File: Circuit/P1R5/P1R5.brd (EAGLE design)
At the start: 50.8 x 50.8 mm, 182 parts, among them J1 2X5_0.05"_CORTEX_DEBUGTH_NOKE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, U1 MK20DX256VLH7, U2 TPS61200, U3 PCA9552BS, U4 PCA9552BS, U5 MPU-9250, U6 ESP8266EX, U7 25Q40, U8 NRF24L01, Y1 8MHz, Y2 34.728kHz, Y3 26 Mhz, Y4 16 Mhz

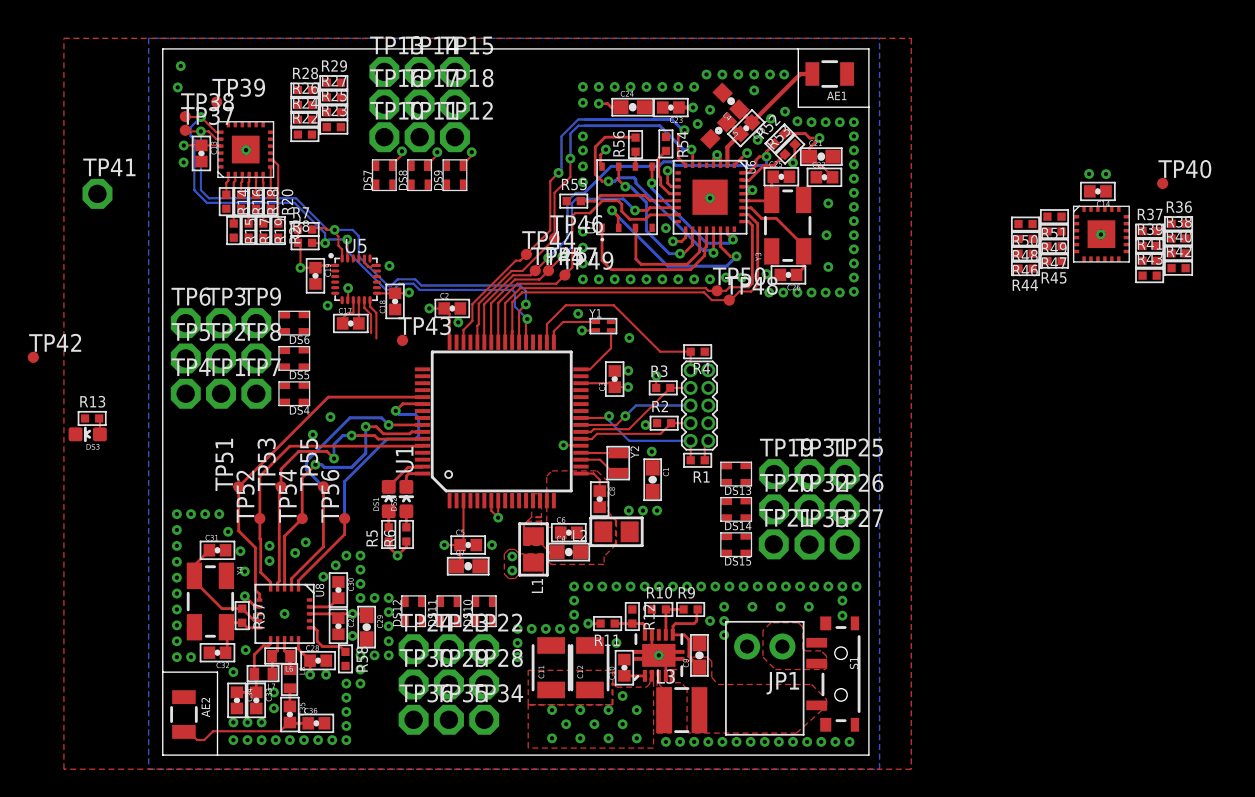
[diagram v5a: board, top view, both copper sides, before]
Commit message: More board layout. Renumbered x+ and y+ to match what I did on the PCB.
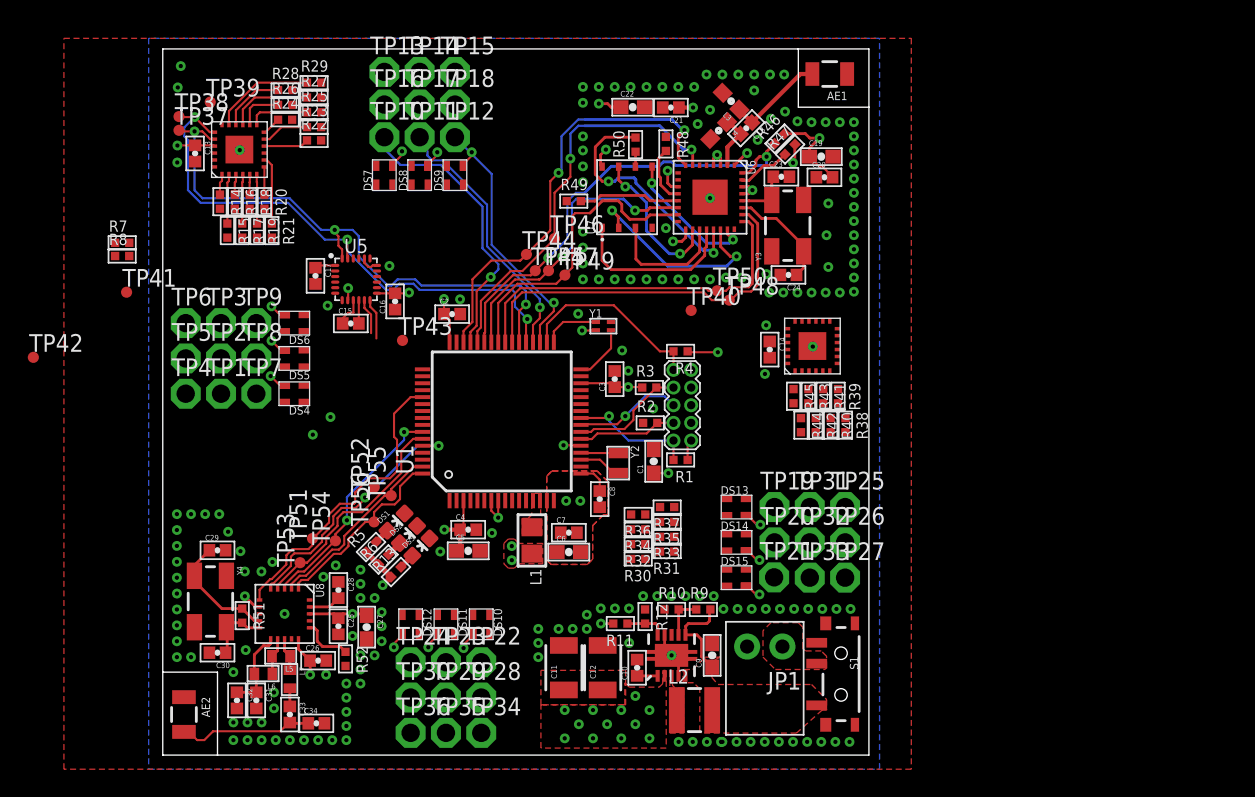
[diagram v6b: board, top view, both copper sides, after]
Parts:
- removed C35: 1.5 pF, SparkFun-Capacitors:0402-CAP
- removed C36: 1.0 pF, SparkFun-Capacitors:0402-CAP
- removed L8: 3.9 nH, SparkFun-Passives:C0402
- removed R53, R54: 12k, appfruits:_0402
- removed R55: 10k, appfruits:_0402
- removed R56: 200, appfruits:_0402
- removed R57: 1M, appfruits:_0402
- removed R58: 22k, appfruits:_0402
- added C15, C16: 0.1 uF, SparkFun-Capacitors:0402-CAP
- added R30, R31, R32, R33, R34, R35: 86.6, appfruits:_0402
- C18: value 0.1 uF -> 5.6 pF
- C19, C22, C27: value 0.1 uF -> 10uF; device SparkFun-Capacitors:0402-CAP -> SparkFun-Capacitors:0603-CAP
- C20: value 5.6 pF -> 0.1 uF
- C21: value 10uF -> 0.1 uF; device SparkFun-Capacitors:0603-CAP -> SparkFun-Capacitors:0402-CAP
- C23: value 0.1 uF -> 15 pF
- C24: value 10uF -> 15 pF; device SparkFun-Capacitors:0603-CAP -> SparkFun-Capacitors:0402-CAP
- C25, C26: value 15 pF -> 0.1 uF
- C28: value 0.1 uF -> .033 uF
- C29: value 10uF -> 22 pF; device SparkFun-Capacitors:0603-CAP -> SparkFun-Capacitors:0402-CAP
- C30: value .033 uF -> 22 pF
- C31: value 22 pF -> 2200 pF
- C32: value 22 pF -> 4.7 pF
- C33: value 2200 pF -> 1.5 pF
- C34: value 4.7 pF -> 1.0 pF
- C4, C7: value 10uF -> 0.1uF; device SparkFun-Capacitors:0603-CAP -> SparkFun-Capacitors:0402-CAP
- C5, C6: value 0.1uF -> 10uF; device SparkFun-Capacitors:0402-CAP -> SparkFun-Capacitors:0603-CAP
- L2: value 600 Ohm/100 Mhz -> 2.2uH, 1.4A; device appfruits:0805 -> appfruits:LPS3015
- L3: value 2.2uH, 1.4A -> DNP; device appfruits:LPS3015 -> SparkFun-Passives:0603
- L5: value DNP -> 8.2 nH; device SparkFun-Passives:0603 -> SparkFun-Passives:C0402
- L6: value 8.2 nH -> 2.7 nH
- L7: value 2.7 nH -> 3.9 nH
- R46, R47, R48: value 86.6 -> 12k
- R49: value 86.6 -> 10k
- R50: value 86.6 -> 200
- R51: value 86.6 -> 1M
- R52: value 12k -> 22k
- TP41: value TPPAD1-13 -> TPTP08R; device testpad:P1-13 -> testpad:TP08R
- moved R51 65.1 mm to (5.71, 10.0), turned to 270 degrees
- moved L5 49.2 mm to (8.51, 7.11), turned to 180 degrees
- moved R52 48.7 mm to (13.1, 6.92), turned to 270 degrees
- moved C25 45.4 mm to (12.6, 9.27), turned to 270 degrees
- moved R36 44.1 mm to (34.2, 17.3), turned to 180 degrees
- moved L3 43.9 mm to (40.9, 47.0), turned to 135 degrees
- moved C26 43.8 mm to (11.2, 6.79), turned to 0 degrees
- moved R37 40.0 mm to (36.3, 17.8), turned to 180 degrees
- moved C19 37.4 mm to (47.4, 43.1), turned to 0 degrees
- moved TP40 35.1 mm to (38.0, 32.0)
- moved R49 34.7 mm to (29.6, 39.9), turned to 0 degrees
- moved R50 28.6 mm to (34.0, 43.9), turned to 90 degrees
- moved R42 28.4 mm to (47.0, 23.7), turned to 270 degrees
- moved C18 28.2 mm to (42.0, 45.1), turned to 225 degrees
- moved R40 27.9 mm to (48.0, 23.7), turned to 270 degrees
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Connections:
- removed net AGND: C4.2, C6.2, C8.2, L2.2, U1.15, U1.16
- net !CS: now also U1.49; no longer U1.45
- net !RESET0: now also U1.55; no longer U1.26
- net 3.3V: now also C16.2, C17.1, C20.2, C22.1, C25.1, C26.1, C4.1, R46.2; no longer C18.2, C22.2, C23.1, C24.1, C28.1, C29.1, C7.1, R52.2
- net CE: now also U1.64; no longer U1.54
- net CLK: now also R50.1; no longer R56.1
- net CSN: now also U1.63; no longer U1.57
- net FSYNC: now also U1.56; no longer U1.36
- net GND: now also C15.1, C16.1, C17.2, C20.1, C22.2, C28.1, C30.2, C4.2, C6.2, C8.2, L3.2, R47.2, R48.1, R49.1, R52.2, U1.15, U1.16; no longer C17.1, C18.1, C22.1, C28.2, C30.1, C33.2, C36.2, L2.1, L5.2, R53.2, R54.1, R55.1, R58.2
- net INT: now also U1.54; no longer U1.35
- net N$10: now also U1.57; no longer U1.63
- net N$100: now also C23.1; no longer C25.1
- net N$101: now also C18.1, L3.1; no longer C20.1, L4.1
- net N$102: now also R48.2; no longer R54.2
- net N$103: now also R49.2; no longer R55.2
- net N$107: now also R47.1; no longer R53.1
- net N$108: now also C29.1, R51.1; no longer C31.1, R57.1
- net N$109: now also C30.1, R51.2; no longer C32.1, R57.2
- net N$111: now also L5.1, L7.1; no longer L6.1, L8.1
- net N$112: now also R52.1; no longer R58.1
- net N$113: now also C28.2; no longer C30.2
- net N$114: now also L5.2, L6.1; no longer L6.2, L7.1
- net N$115: now also C33.2, C34.1; no longer C35.2, C36.1
- net N$116: now also C33.1, L7.2; no longer C35.1, L8.2
- net N$117: now also C31.1, C32.1, L6.2; no longer C33.1, C34.1, L7.2
- net N$12: now also U1.45; no longer U1.62
- net N$13: now also U1.61; no longer U1.64
- net N$14: now also U1.36; no longer U1.61
- net N$15: now also U1.35; no longer U1.49
- net N$16: now also U1.62; no longer U1.56
- net N$17: now also U1.26; no longer U1.55
- net N$18: now also U1.2; no longer U1.1
- net N$19: now also U1.1; no longer U1.2
- net N$22: now also C18.2, L4.1; no longer C20.2, L5.1
- net N$23: now also C24.1; no longer C26.1
- net N$24: now also L2.1; no longer L3.1
- net N$3: now also R50.2; no longer R56.2
- net N$4: now also C15.2; no longer C17.2
- net N$42: now also R31.2; no longer R37.2
- net N$43: now also R30.2; no longer R36.2
- net N$50: now also R40.2; no longer R46.2
- net N$52: now also R33.2; no longer R39.2
- net N$57: now also R45.2; no longer R51.2
- net N$58: now also R35.2; no longer R41.2
- net N$59: now also R39.2; no longer R45.2
- net N$61: now also R34.2; no longer R40.2
- net N$62: now also R42.2; no longer R48.2
- net N$63: now also R32.2; no longer R38.2
- net N$64: now also R37.2; no longer R43.2
- net N$67: now also R41.2; no longer R47.2
- net N$68: now also R38.2; no longer R44.2
- net N$70: now also R43.2; no longer R49.2
- net N$82: now also R36.2; no longer R42.2
- net N$83: now also R44.2; no longer R50.2
- net N$84: now also R30.1; no longer R36.1
- net N$85: now also R31.1; no longer R37.1
- net N$86: now also R32.1; no longer R38.1
- net N$87: now also R33.1; no longer R39.1
- net N$88: now also R34.1; no longer R40.1
- net N$89: now also R35.1; no longer R41.1
- net N$90: now also R36.1; no longer R42.1
- net N$91: now also R37.1; no longer R43.1
- net N$92: now also R38.1; no longer R44.1
- net N$93: now also R39.1; no longer R45.1
- net N$94: now also R40.1; no longer R46.1
- net N$95: now also R41.1; no longer R47.1
- net N$96: now also R42.1; no longer R48.1
- net N$97: now also R43.1; no longer R49.1
- net N$98: now also R44.1; no longer R50.1
- net N$99: now also R45.1; no longer R51.1
- net VDDA: now also C7.1; no longer C4.1
- net V_IN: now also L2.2; no longer L3.2
- net WIFI_RESET: now also R46.1; no longer R52.1
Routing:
- net N$12: track 0.00 -> 20.7 mm, vias 0 -> 1
- net N$14: track 0.00 -> 19.0 mm, vias 0 -> 1
- net N$15: track 0.00 -> 18.3 mm, vias 0 -> 1
- net 3.3V: track 66.6 -> 76.9 mm, vias 43 -> 51
- net N$81: track 0.00 -> 7.43 mm
- net CE: track 21.1 -> 13.9 mm, vias 1 -> 0
- net CSN: track 20.5 -> 13.9 mm, vias 1 -> 0
- net N$79: track 0.00 -> 6.06 mm
- net N$80: track 0.00 -> 4.66 mm
- net MOSI: track 21.0 -> 16.6 mm, vias 2 -> 0
- net N$77: track 0.00 -> 4.36 mm
- net SCK: track 20.2 -> 16.5 mm
- net N$75: track 0.00 -> 3.42 mm
- net N$78: track 0.00 -> 3.30 mm
- net N$74: track 0.00 -> 3.23 mm
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- added copper zone on layer 1, net N$1000
- removed copper zone on layer 1, net AGND

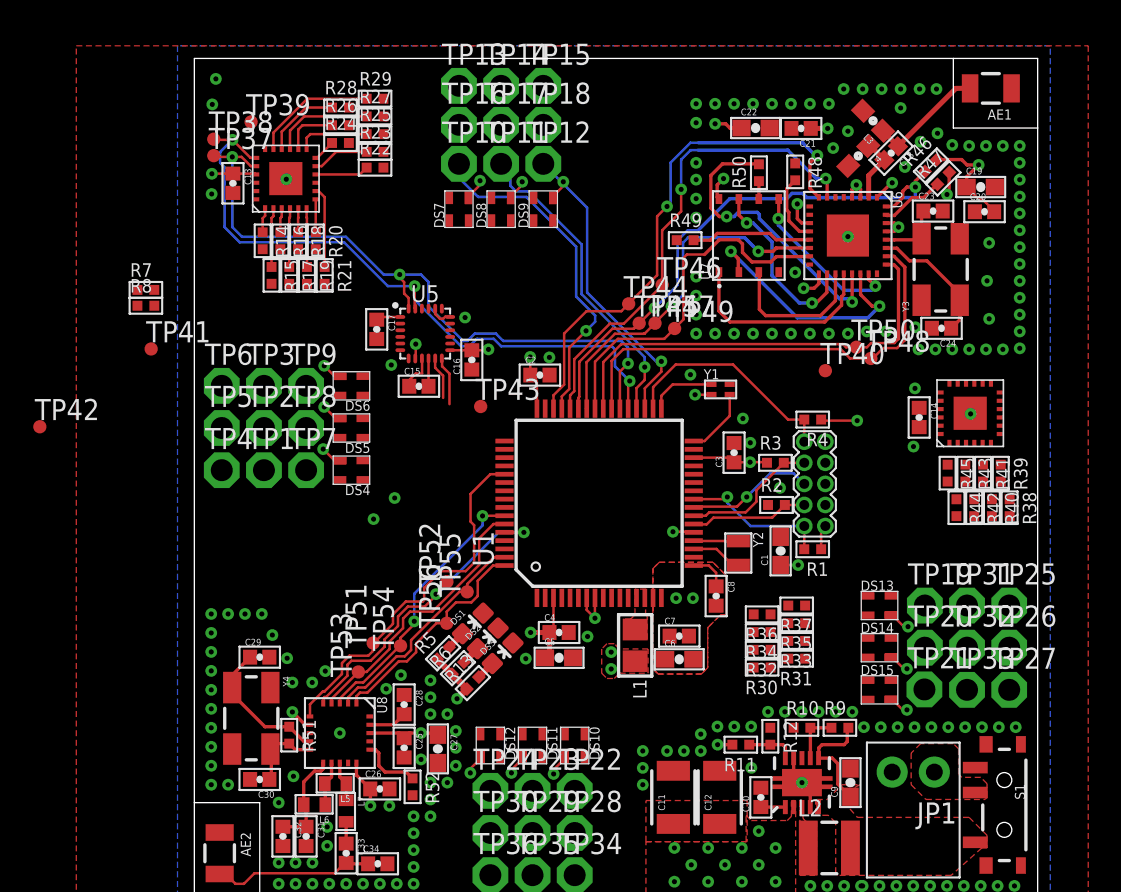
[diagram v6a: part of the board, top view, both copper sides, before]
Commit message: Everything but 3 banks of LED's is routed.
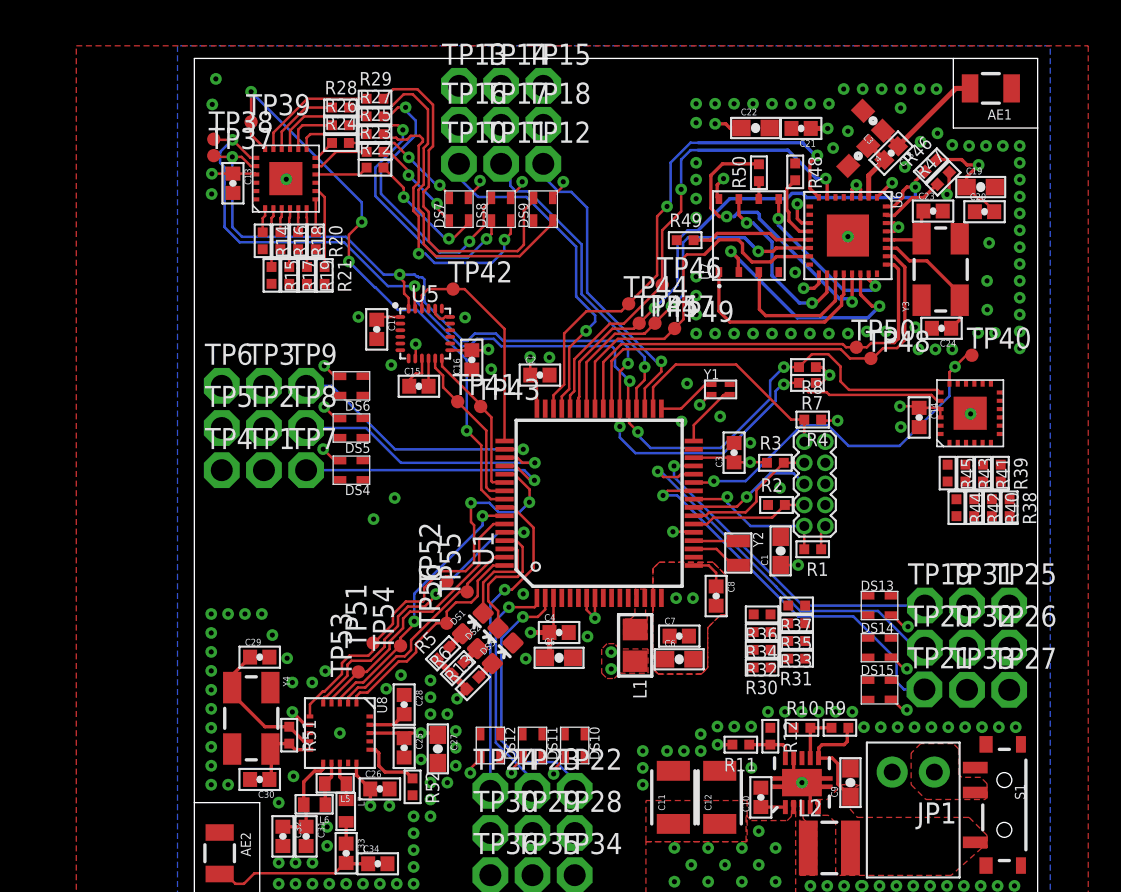
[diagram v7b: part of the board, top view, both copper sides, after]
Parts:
- moved R7 40.2 mm to (36.9, 31.3), turned to 180 degrees
- moved R8 40.0 mm to (36.9, 32.2), turned to 180 degrees
- moved TP42 26.2 mm to (15.6, 36.9)
- moved TP41 18.7 mm to (15.9, 30.1)
- moved TP40 8.88 mm to (46.8, 32.9)
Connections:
- net !RESET0: now also U1.56; no longer U1.55
- net 3.3V: now also DS10.4, DS11.4, DS12.4, DS13.4, DS14.4, DS15.4, DS4.4, DS5.4, DS6.4, DS7.4, DS8.4, DS9.4; no longer DS10.V, DS11.V, DS12.V, DS13.V, DS14.V, DS15.V, DS4.V, DS5.V, DS6.V, DS7.V, DS8.V, DS9.V
- net FSYNC: now also U1.55; no longer U1.56
- net N$10: now also U1.62; no longer U1.57
- net N$16: now also U1.57; no longer U1.62
- net N$20: now also TP19.TP; no longer TP20.TP
- net N$21: now also TP20.TP; no longer TP19.TP
- net N$36: now also DS8.2; no longer DS8.R
- net N$37: now also DS7.2; no longer DS7.R
- net N$38: now also DS7.1; no longer DS7.B
- net N$39: now also DS7.3; no longer DS7.G
- net N$40: now also DS8.1; no longer DS8.B
- net N$41: now also DS8.3; no longer DS8.G
- net N$42: now also DS10.3; no longer DS10.G
- net N$43: now also DS10.1; no longer DS10.B
- net N$44: now also DS9.1; no longer DS9.B
- net N$45: now also DS9.3; no longer DS9.G
- net N$47: now also DS5.2; no longer DS5.R
- net N$50: now also DS14.1; no longer DS14.B
- net N$51: now also DS4.2; no longer DS4.R
- net N$52: now also DS11.2; no longer DS11.R
- net N$53: now also DS4.1; no longer DS4.B
- net N$54: now also DS4.3; no longer DS4.G
- net N$55: now also DS5.1; no longer DS5.B
- net N$56: now also DS5.3; no longer DS5.G
- net N$57: now also DS15.3; no longer DS15.G
- net N$58: now also DS12.1; no longer DS12.B
- net N$59: now also DS13.3; no longer DS13.G
- net N$61: now also DS11.3; no longer DS11.G
- net N$62: now also DS14.3; no longer DS14.G
- net N$63: now also DS11.1; no longer DS11.B
- net N$64: now also DS12.3; no longer DS12.G
- net N$65: now also DS6.1; no longer DS6.B
- net N$66: now also DS6.3; no longer DS6.G
- net N$67: now also DS14.2; no longer DS14.R
- net N$68: now also DS13.1; no longer DS13.B
- net N$70: now also DS15.1; no longer DS15.B
- net N$82: now also DS12.2; no longer DS12.R
- net N$83: now also DS15.2; no longer DS15.R
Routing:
- net !RESET0: track 0.00 -> 36.5 mm, vias 0 -> 4
- net SCL: track 41.5 -> 66.3 mm, vias 3 -> 5
- net SDA: track 41.3 -> 65.2 mm, vias 3 -> 5
- net N$17: track 0.00 -> 23.3 mm, vias 0 -> 1
- net N$45: track 0.00 -> 23.0 mm
- net !RESET1: track 0.00 -> 23.0 mm, vias 0 -> 2
- net N$21: track 0.00 -> 22.9 mm, vias 0 -> 1
- net N$44: track 0.00 -> 21.4 mm
- net N$20: track 0.00 -> 20.2 mm, vias 0 -> 1
- net N$16: track 0.00 -> 19.4 mm, vias 0 -> 1
- net N$40: track 0.00 -> 18.2 mm, vias 0 -> 2
- net N$36: track 0.00 -> 18.0 mm, vias 0 -> 2
- net N$41: track 0.00 -> 17.6 mm, vias 0 -> 2
- net N$6: track 0.00 -> 16.6 mm, vias 0 -> 1
- net N$18: track 0.00 -> 16.3 mm, vias 0 -> 1
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
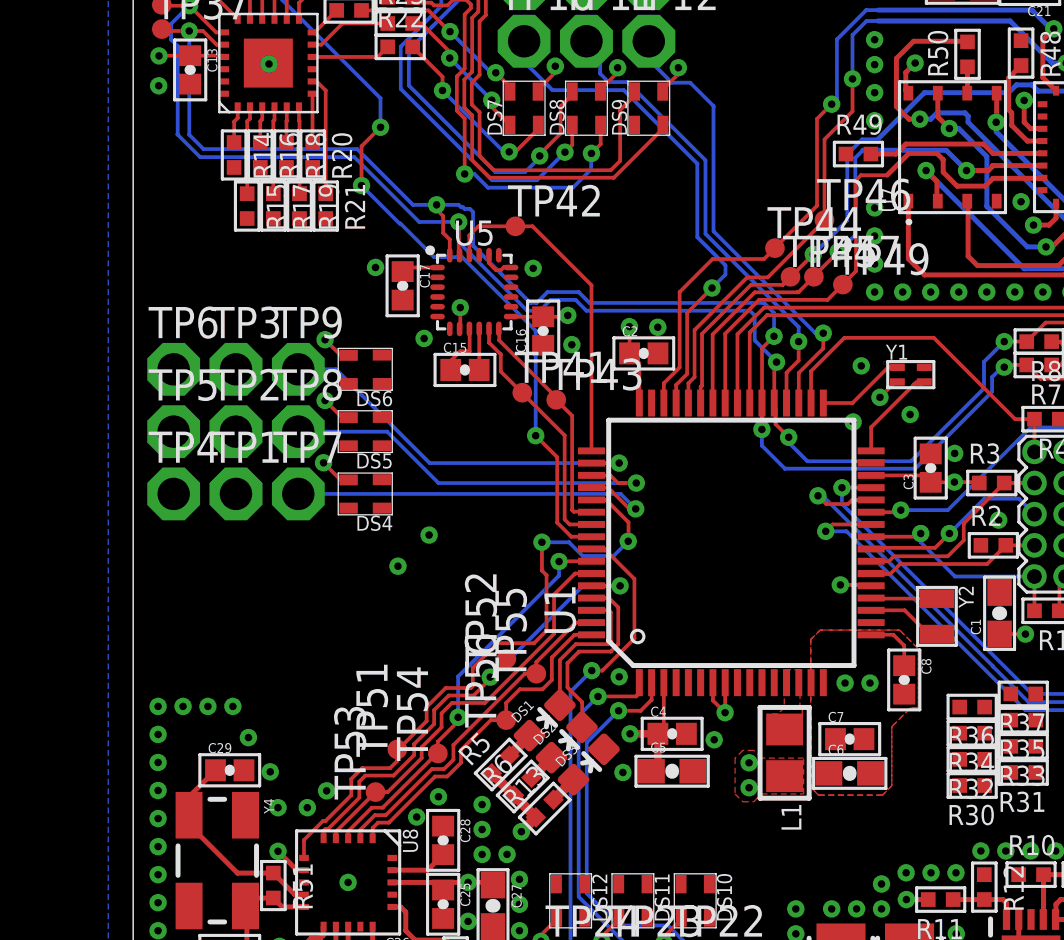
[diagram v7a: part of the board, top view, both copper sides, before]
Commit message: Routed another bank of LED's moved IMU up and to the right a bit.
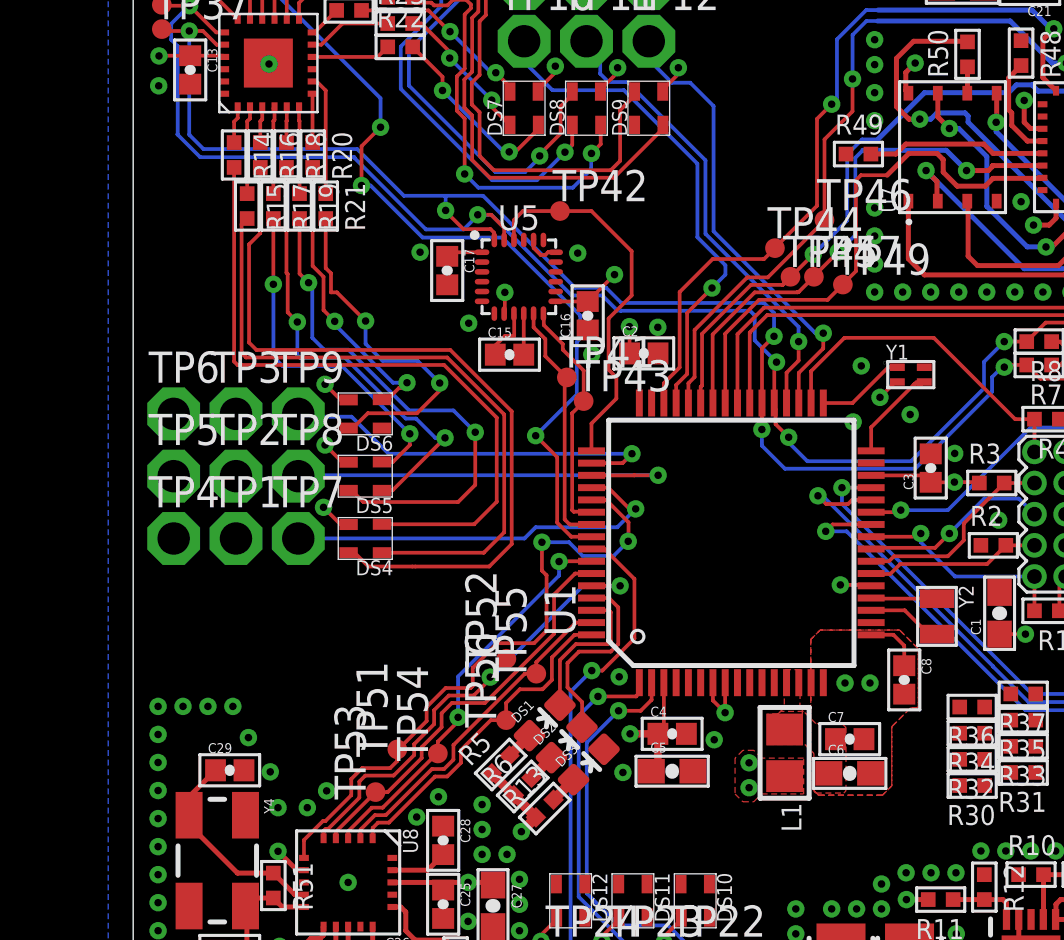
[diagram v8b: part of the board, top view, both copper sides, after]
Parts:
- moved C17 1.92 mm to (12.8, 35.1)
- moved TP42 1.92 mm to (17.4, 37.5)
- moved C15 1.92 mm to (15.3, 31.7)
- moved TP41 1.92 mm to (17.7, 30.7)
- moved U5 1.92 mm to (15.7, 34.8)
- moved C16 1.92 mm to (18.5, 33.3)
- moved DS4 1.82 mm to (9.46, 24.2)
- moved DS5 1.82 mm to (9.46, 26.7)
- moved DS6 1.82 mm to (9.46, 29.3)
- moved TP1 1.82 mm to (4.19, 24.2)
- moved TP2 1.82 mm to (4.19, 26.7)
- moved TP3 1.82 mm to (4.19, 29.3)
- moved TP4 1.82 mm to (1.65, 24.2)
- moved TP5 1.82 mm to (1.65, 26.7)
- moved TP6 1.82 mm to (1.65, 29.3)
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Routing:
- net N$53: track 0.00 -> 31.9 mm
- net N$54: track 0.00 -> 28.1 mm
- net N$51: track 0.00 -> 27.5 mm
- net N$55: track 0.00 -> 21.1 mm, vias 0 -> 2
- net N$47: track 0.00 -> 18.7 mm, vias 0 -> 2
- net N$56: track 0.00 -> 14.4 mm, vias 0 -> 2
- net N$65: track 0.00 -> 14.3 mm, vias 0 -> 2
- net N$66: track 0.00 -> 12.0 mm, vias 0 -> 2
- net !RESET0: track 36.5 -> 39.4 mm
- net !CS: track 13.7 -> 15.5 mm
- net N$6: track 16.6 -> 17.4 mm
- net 3.3V: track 80.7 -> 81.2 mm
- net GND: vias 187 -> 185
